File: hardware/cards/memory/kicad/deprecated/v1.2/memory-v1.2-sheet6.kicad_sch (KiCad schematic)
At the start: 7 parts, among them IC14 74*04, IC15 74*374, IC16 74*374, IC17 74*374, IC19 74*374

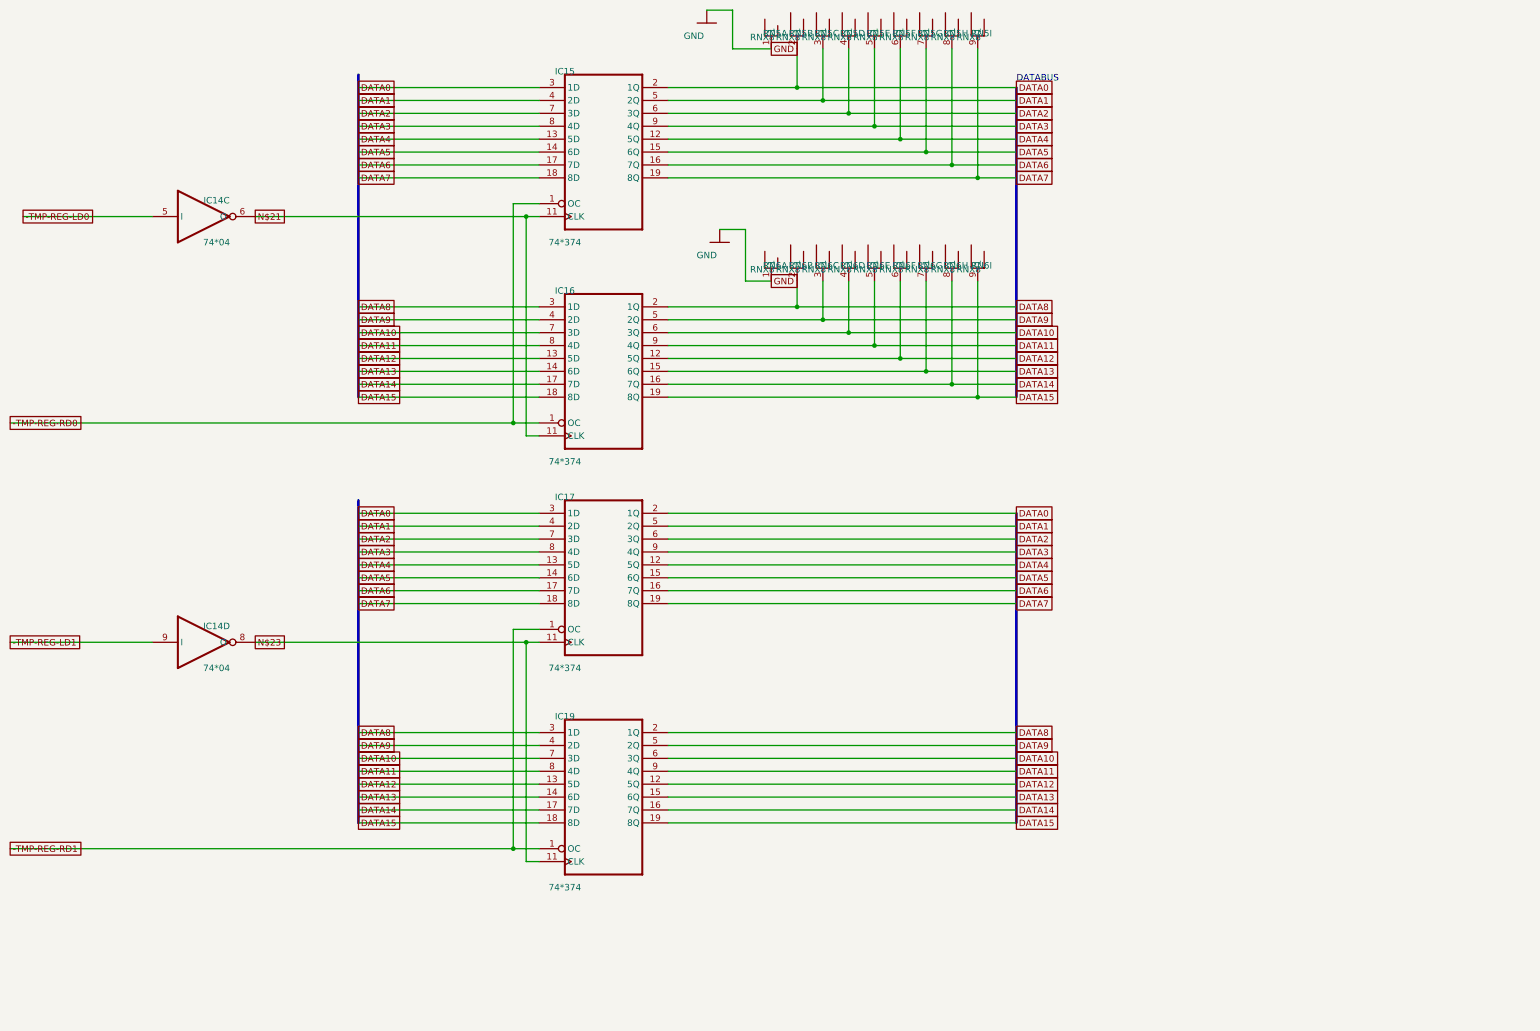
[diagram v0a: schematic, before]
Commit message: fix(kicad): readable converted schematics - overlaps 42,847 -> 3,147, nothing off the frame; CF sheet 0 overlaps
- tools/kicad/sch_overlaps.py: calibrated readability check (text/text, text/body, text/line, off frame/title block)
- eagle_sch_to_kicad.py: fields placed from Eagle's smashed attributes or the symbol's >NAME/>VALUE with Eagle's align,
  size and ratio, readable angles; fields Eagle never shows hidden (FABC96R shows only its pin name); pin numbers hidden
  where every Eagle pin hides them; Eagle-hidden layers dropped (the stray SpiceOrder text); labels on their own wires,
  converter labels only where KiCad needs them; rotate-then-mirror fixed for MR90/MR270 in pin_world/no-connects;
  each sheet on the smallest page that holds it, centred clear of the title block
- finish_board.py: stable footprint-library choice (DRC counts no longer vary run to run)
- all 37 projects regenerated: netlist proofs unchanged (34 MATCH, 2 schematic-only, video Fusion export MISMATCH as
  before); DRC same or better; ERC up (loose wire ends onto graphic buses no longer hidden by labels; explained per README)
- CF card: gate names off the gate bodies, U3 clear of its title, 5.08 mm connector pins; rebuilt: DRC 0/0, proof MATCH
- schematic PDFs regenerated (tools/sch_to_pdf.py, 37/37)

Co-Authored-By: Claude Opus 5.5 <noreply@anthropic.com>
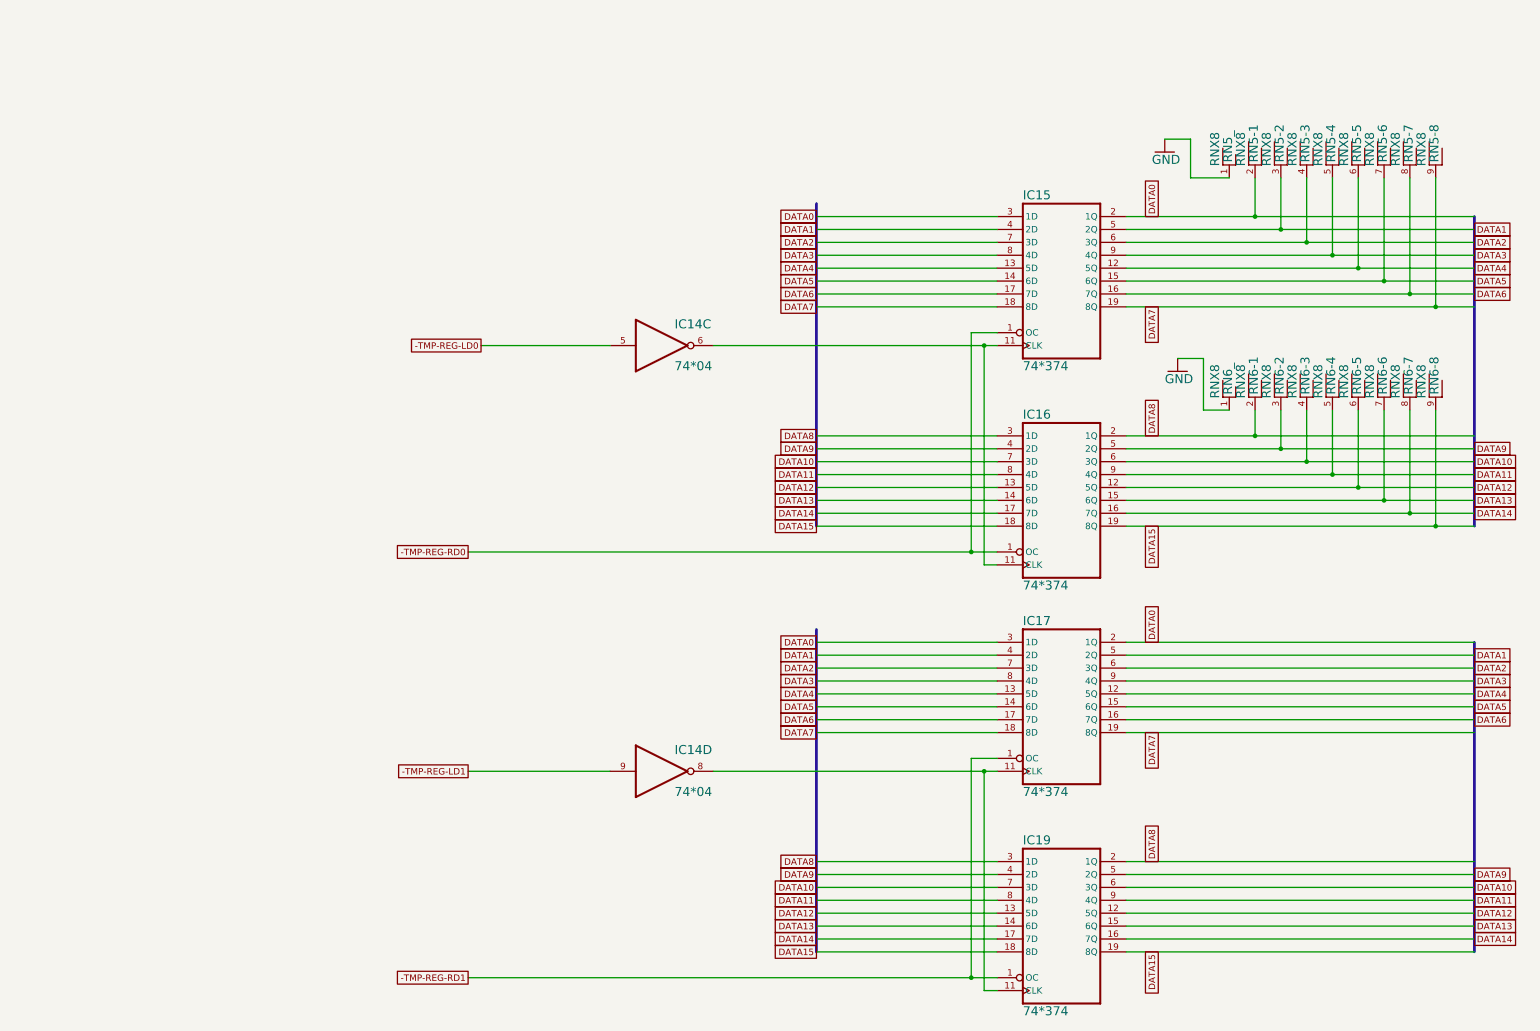
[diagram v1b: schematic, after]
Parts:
- RN5: Eagle name (none) -> RN5-4
- RN5: Eagle name (none) -> RN5-5
- RN5: Eagle name (none) -> RN5-2
- RN5: Eagle name (none) -> RN5-1
- RN5: Eagle name (none) -> RN5_
- RN5: Eagle name (none) -> RN5-7
- RN5: Eagle name (none) -> RN5-6
- RN5: Eagle name (none) -> RN5-8
- RN5: Eagle name (none) -> RN5-3
- RN6: Eagle name (none) -> RN6-3
- RN6: Eagle name (none) -> RN6-7
- RN6: Eagle name (none) -> RN6-1
- RN6: Eagle name (none) -> RN6-4
- RN6: Eagle name (none) -> RN6_
- RN6: Eagle name (none) -> RN6-6
- RN6: Eagle name (none) -> RN6-2
- RN6: Eagle name (none) -> RN6-8
- RN6: Eagle name (none) -> RN6-5
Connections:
- net N$21: no longer names the net of IC14.6 (O), IC15.11 (CLK), IC16.11 (CLK)
- net N$23: no longer names the net of IC14.8 (O), IC17.11 (CLK), IC19.11 (CLK)
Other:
- note removed: "DATABUS"
- moved on the sheet: IC15, IC16, IC17, IC19
